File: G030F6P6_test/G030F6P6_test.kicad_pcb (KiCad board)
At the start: 2 copper layers, 22.9 x 49.1 mm, 28 parts, among them J1 Conn_01x10_Female, J3 Conn_01x10_Female, J4 USB_C_Receptacle_USB2.0, J5 Conn_01x05_Female, U1 CH343P, U2 STM32G030FxP, U3 XC6206P332MR

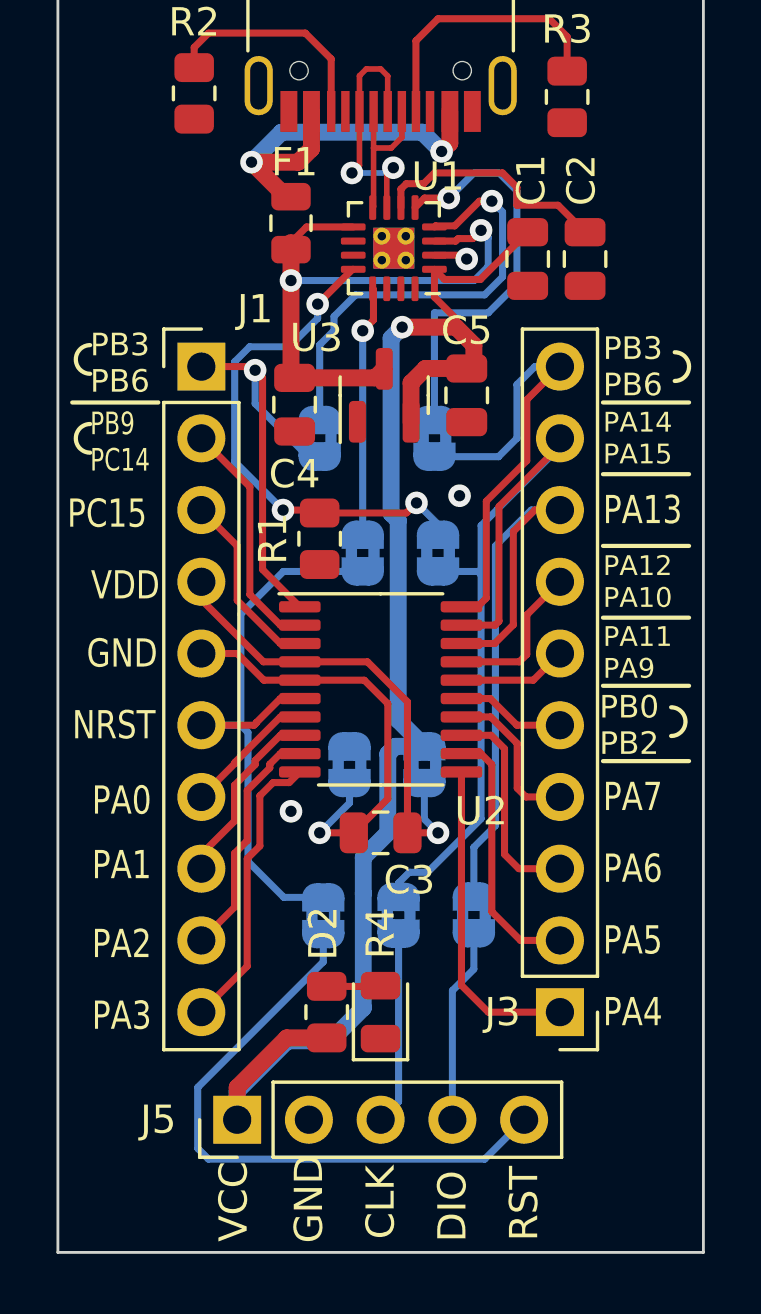
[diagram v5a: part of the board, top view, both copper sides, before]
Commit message: 調整腳位位置
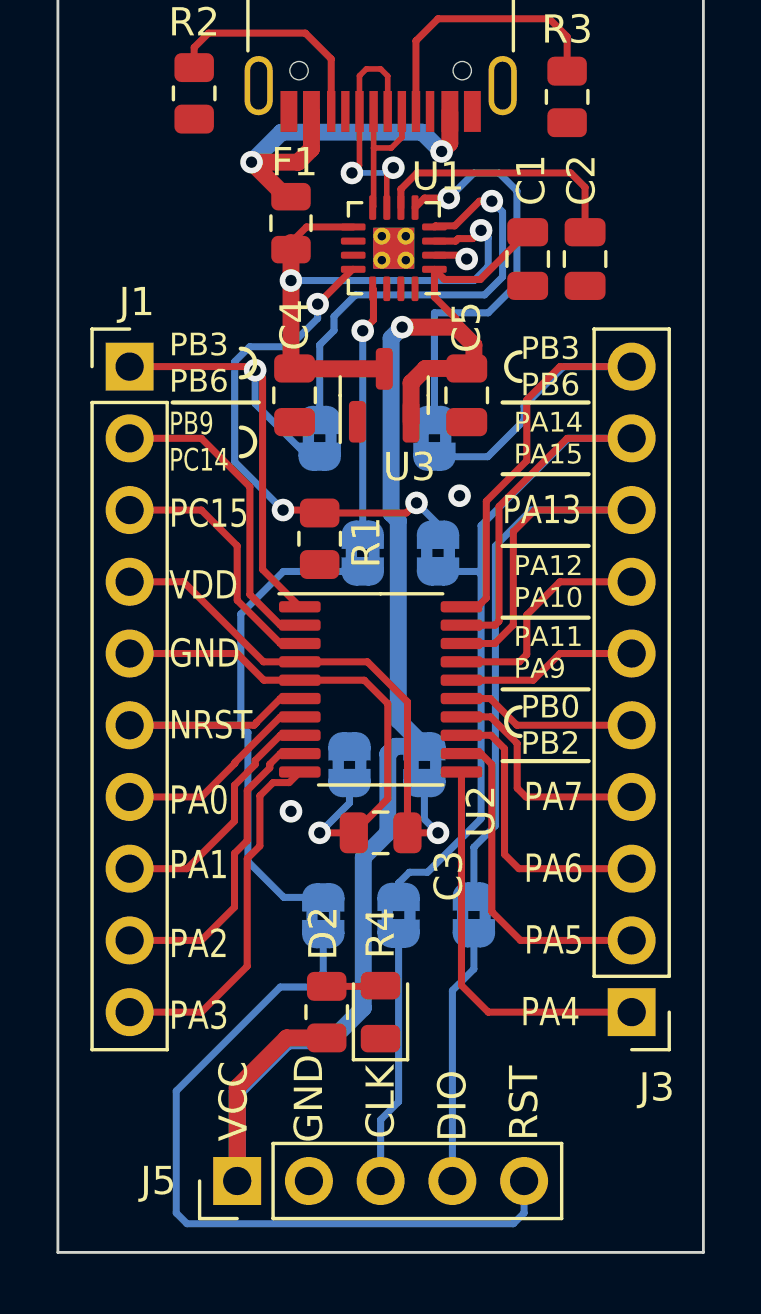
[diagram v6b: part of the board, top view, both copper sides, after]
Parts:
- moved J1 2.54 mm to (121.9, 73.7)
- moved J3 2.54 mm to (139.7, 96.5)
- moved J5 2.17 mm to (125.7, 102.5)
- moved C4 0.33 mm to (127.8, 74.7)
- moved REF** 0.13 mm to (122.8, 63.0)
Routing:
- net /PIN6: track 22.3 -> 27.4 mm
- net /PIN18: track 22.9 -> 28.0 mm
- net /PIN19: track 29.3 -> 34.1 mm
- net /NRST: track 21.7 -> 26.4 mm
- net +3V3: track 52.0 -> 56.3 mm
- net /PIN20: track 17.2 -> 21.4 mm
- net /PIN13: track 7.64 -> 10.2 mm
- net /PIN15: track 3.88 -> 6.42 mm
- net /PIN9: track 8.46 -> 11.0 mm
- net /PIN7: track 4.68 -> 7.22 mm
- net /PIN5: track 15.8 -> 18.4 mm
- net /PIN2: track 8.46 -> 11.0 mm
- net /PIN17: track 5.48 -> 8.02 mm
- net /PIN16: track 3.88 -> 6.42 mm
- net /PIN14: track 5.59 -> 8.13 mm
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
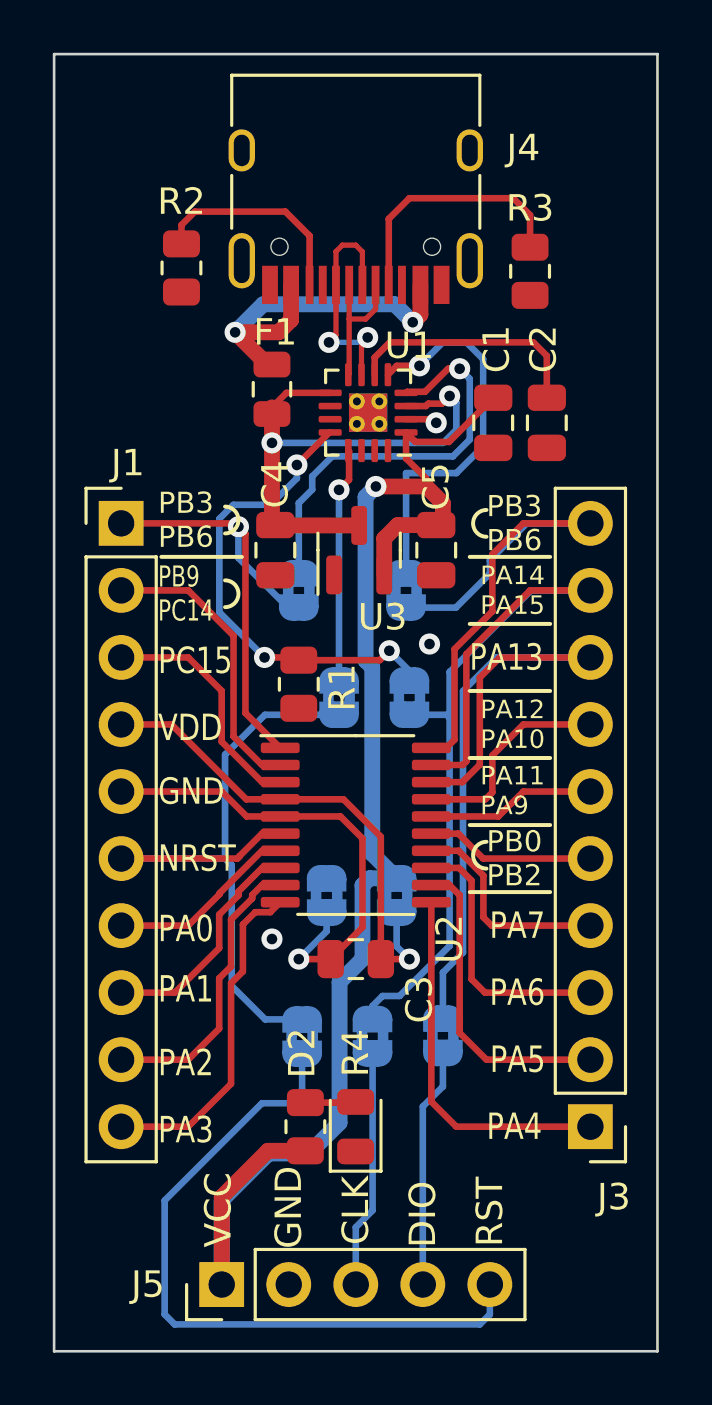
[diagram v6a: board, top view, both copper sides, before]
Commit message: 調整細節
增加 5V 腳位封裝
調整部分位置
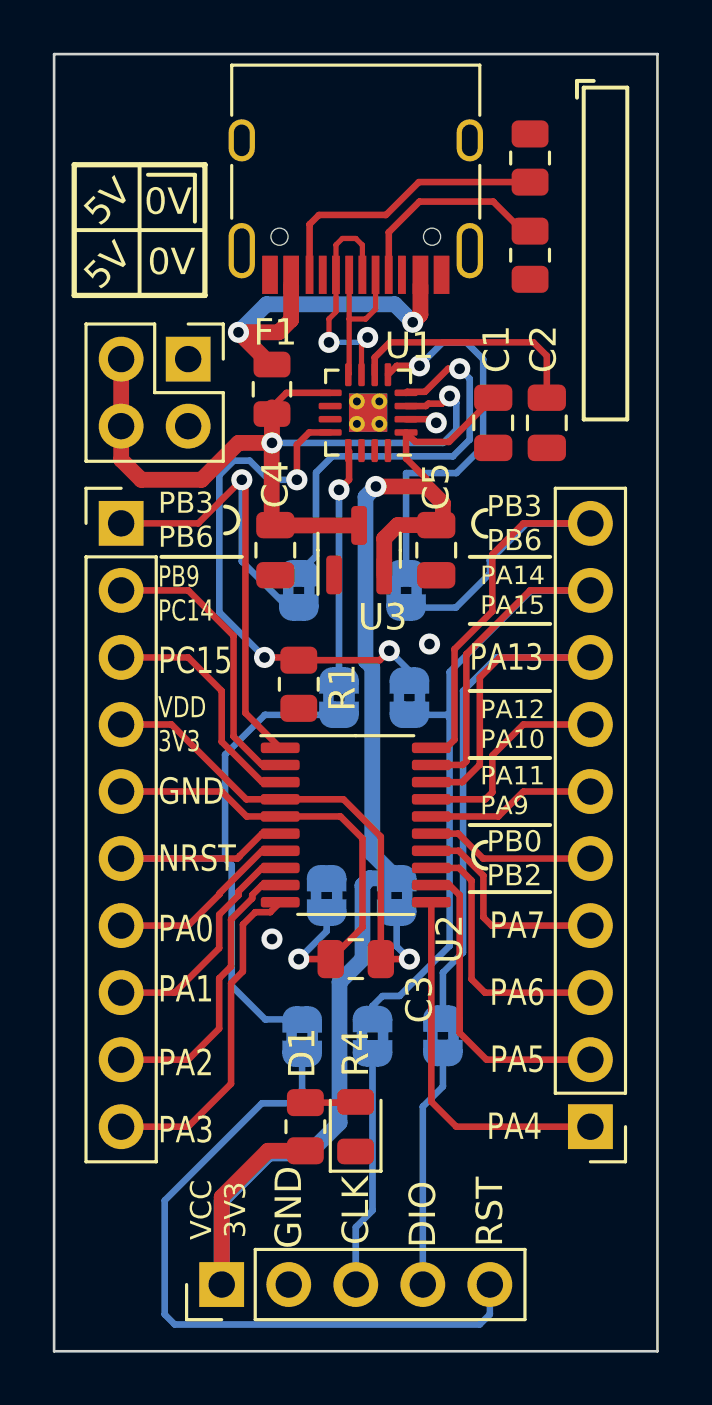
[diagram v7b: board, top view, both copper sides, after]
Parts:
- added J4: Conn_02x02_Odd_Even, Connector_PinSocket_2.54mm:PinSocket_2x02_P2.54mm_Vertical, F.Cu at (124.5, 67.4)
- moved REF** 15.7 mm to (138.6, 63.0)
- moved R2 13.8 mm to (137.4, 59.8), turned to -90 degrees
- moved R3 0.61 mm to (137.4, 63.5)
- moved J3 0.38 mm to (130.8, 60.2)
- renumbered D2 to D1, J3 to J2, J4 to J3
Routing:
- net VBUS: track 20.5 -> 30.9 mm
- net /PIN1: track 17.8 -> 22.0 mm
- net /CC2: track 8.02 -> 10.9 mm
- net /BOOT0: track 18.2 -> 20.2 mm
- net /CC1: track 9.66 -> 7.91 mm
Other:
- board text added: "0V"
- board text added: "5V"
- board text added: "VCC 3V3"
- board text added: "VDD 3V3"
- board text removed: "VDD"
